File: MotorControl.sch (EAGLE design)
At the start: 47 parts, among them IC1 ESP32-WROOM-32E8M, IC2 TB6612FNG, U3 TP4056, U4 SPX3940AM3-L-3-3/TR, U5 INTERFACE-FT230XS-R(SSOP16)

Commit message: [fix] シルク作成
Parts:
- removed C17: 4.7uf, OPL_Capacitor:TANTALUM-SMD-4.7UF-16V(AVX-A)
- added C1: 100nf, OPL_Capacitor:CERAMIC-100NF-50V-10%-X7R(0805)
- C10: value 100nF/50V(10%) -> 4.7uf; device OPL_Capacitor:CERAMIC-100NF-50V-10%-X7R(0603) -> OPL_Capacitor:TANTALUM-SMD-4.7UF-16V(AVX-A)
- C2: value 100nf -> 10uf; device OPL_Capacitor:CERAMIC-100NF-50V-10%-X7R(0805) -> OPL_Capacitor:CERAMIC-10UF-25V-10%-X5R(1206)
- C3: value 10uf -> 22uF/16V(10%); device OPL_Capacitor:CERAMIC-10UF-25V-10%-X5R(1206) -> OPL_Capacitor:CERAMIC-22UF-16V-10%-X7R(1206)
- C4: value 22uF/16V(10%) -> 100nf; device OPL_Capacitor:CERAMIC-22UF-16V-10%-X7R(1206) -> OPL_Capacitor:CERAMIC-100NF-50V-10%-X7R(0805)
- C5: value 100nf -> 10nf; device OPL_Capacitor:CERAMIC-100NF-50V-10%-X7R(0805) -> OPL_Capacitor:CERAMIC-10NF-50V-5%-X7R(0805)
- C6: value 10nf -> 100nF/50V(10%); device OPL_Capacitor:CERAMIC-10NF-50V-5%-X7R(0805) -> OPL_Capacitor:CERAMIC-100NF-50V-10%-X7R(0603)
- renumbered BOOT_SW to BOOT-SW, D1 to BAT-RED, D2 to USB-TO-SERIAL-LED, D3 to PWR-LED, D4 to BAT-BLUE, E1 to FERRITE-BEAD, F1 to HUSE, IC1 to ESP32, IC2 to DRIVER-IC, MOTOR_PIN to MOTOR-PIN, POWER_SW to PWR-SW, R13 to R5, U3 to CHARGER-IC, U4 to LDO-IC, U5 to CNV-IC
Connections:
- net +3V3: now also C3.2, C6.2; no longer C4.2, C7.2
- net B+: now also C2.2; no longer C3.2
- net GND: now also C1.1, C10.-, C5.2, C6.1; no longer C10.1, C17.-, C5.1, C6.2
- net N$19: now also C10.+; no longer C17.+
- net N$29: now also C7.2; no longer C10.2
- net N$5: now also C4.2; no longer C5.2
- net VBUS: now also C5.1; no longer C6.1
- net VIN+: now also C1.2; no longer C2.2
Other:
- moved on the sheet: C2, C3, C4, C5, C6, C7

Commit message: [Fix] 20210920MT時点（４層）
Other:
- moved on the sheet: BAT-BLUE, BAT-RED, BOOT-SW, C1, C10, C11, C12, C13, C14, C15, C16, C2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

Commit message: [M] ２面に対応
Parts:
- removed R12, R9: 0.1R, OPL_Resistor:SMD-RES-0.1R-5%-1/8W(0805)
- added C17: 10UF 6.3V, OPL_Capacitor:CERAMIC-10UF-6.3V-20%-X5R(0603)
- added IC1: DW01A, DW01A:DW01A
- added Q1: FS8205A, FS8205A:FS8205A
- C13: value 10uf -> 100nf; device OPL_Capacitor:CERAMIC-10UF-25V-10%-X5R(0805) -> OPL_Capacitor:CERAMIC-100NF-50V-10%-X7R(0805)
- R5: value 0.1R -> 100R; device OPL_Resistor:SMD-RES-0.1R-5%-1/8W(0805) -> OPL_Resistor:SMD-RES-100R-5%-1/4W(1206)
- R8: value 0.1R -> 1K; device OPL_Resistor:SMD-RES-0.1R-5%-1/8W(0805) -> OPL_Resistor:SMD-RES-1K-5%-1/8W(0805)
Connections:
- removed net N$17: R8.2, R9.1
- removed net N$20: R12.2, R5.1
- new net B-: BAT.P$2, C13.2, IC1.GND, Q1.S1
- new net N$1: IC1.OC, Q1.G2
- new net N$10: IC1.OD, Q1.G1
- net B+: now also C17.1, R5.2; no longer C13.2
- net GND: now also C17.2, Q1.S2, R8.2; no longer BAT.P$2, C13.1
- net N$18: now also C13.1, IC1.VCC, R5.1; no longer R12.1, R9.2
- net N$19: now also IC1.CS; no longer C10.+, C16.2, CNV-IC.VCC, FERRITE-BEAD.1, R7.2
- net VIN+: now also C10.+, C16.2, CNV-IC.VCC, FERRITE-BEAD.1, R7.2; no longer R5.2
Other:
- moved on the sheet: BAT, BAT-BLUE, BAT-RED, C1, C13, CHARGER-IC, R2, R3, R5, R8, RPROG

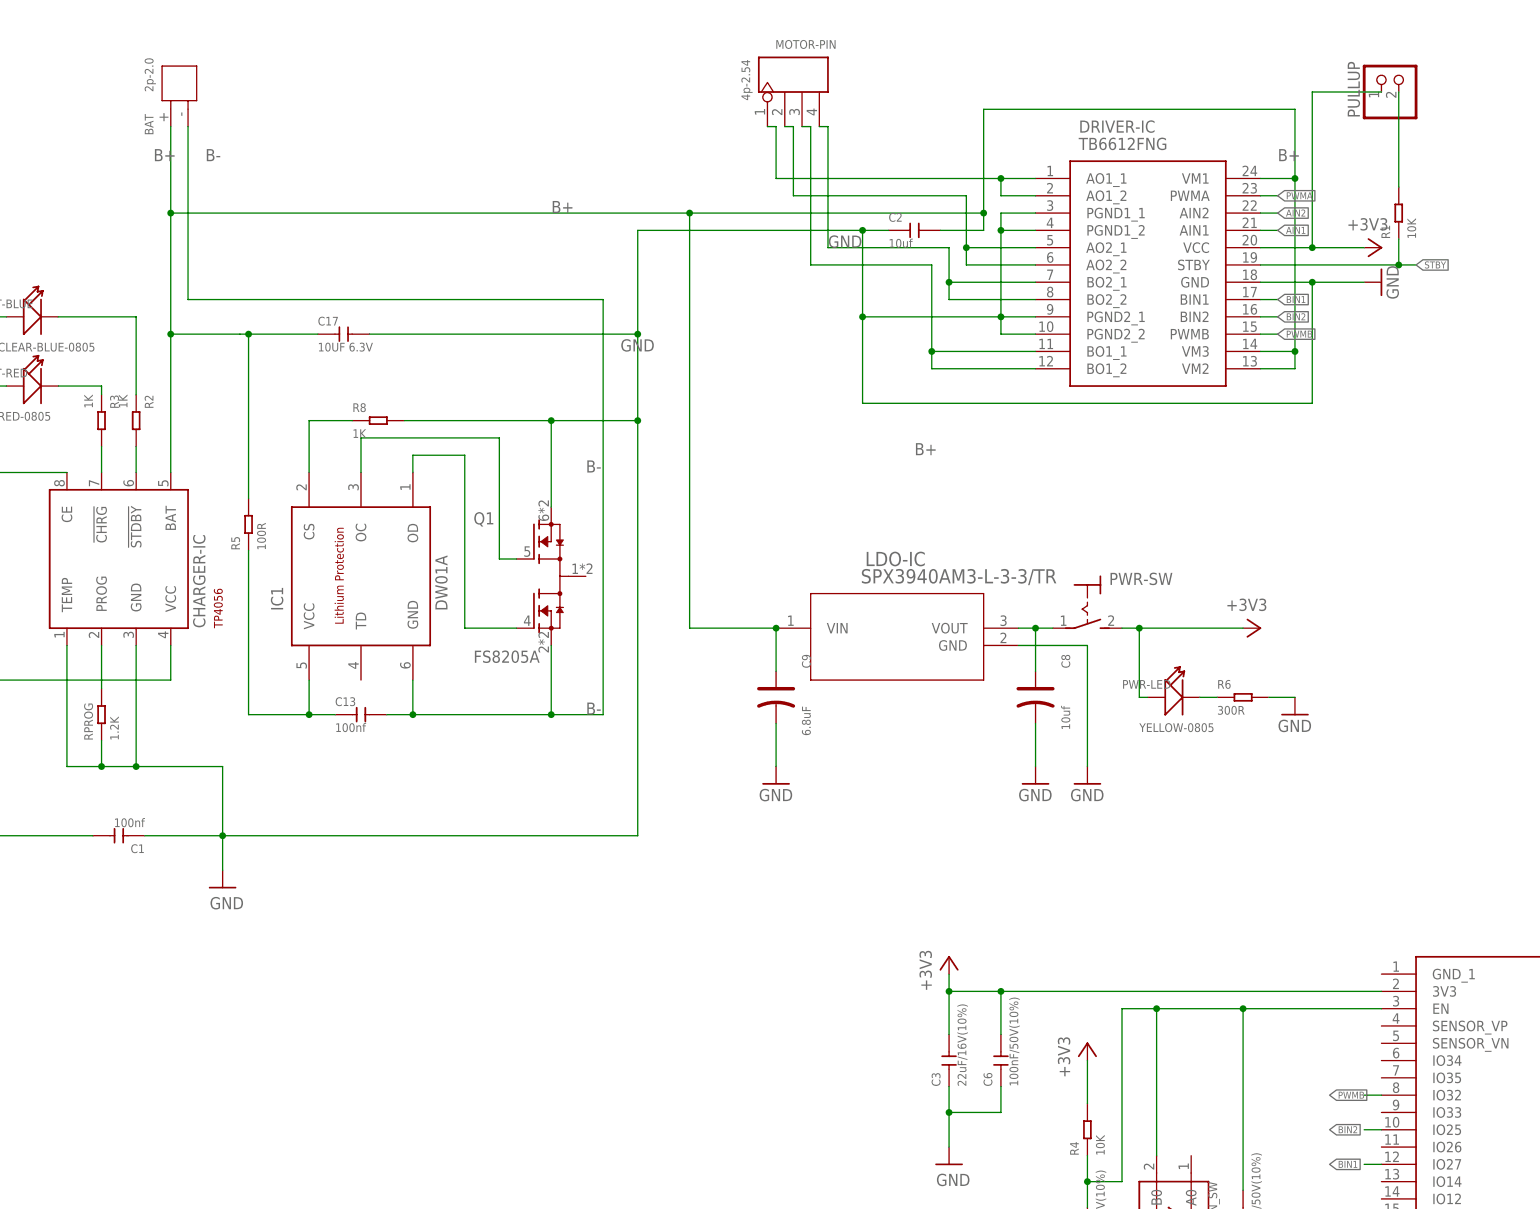
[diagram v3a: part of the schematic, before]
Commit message: [A] add output data
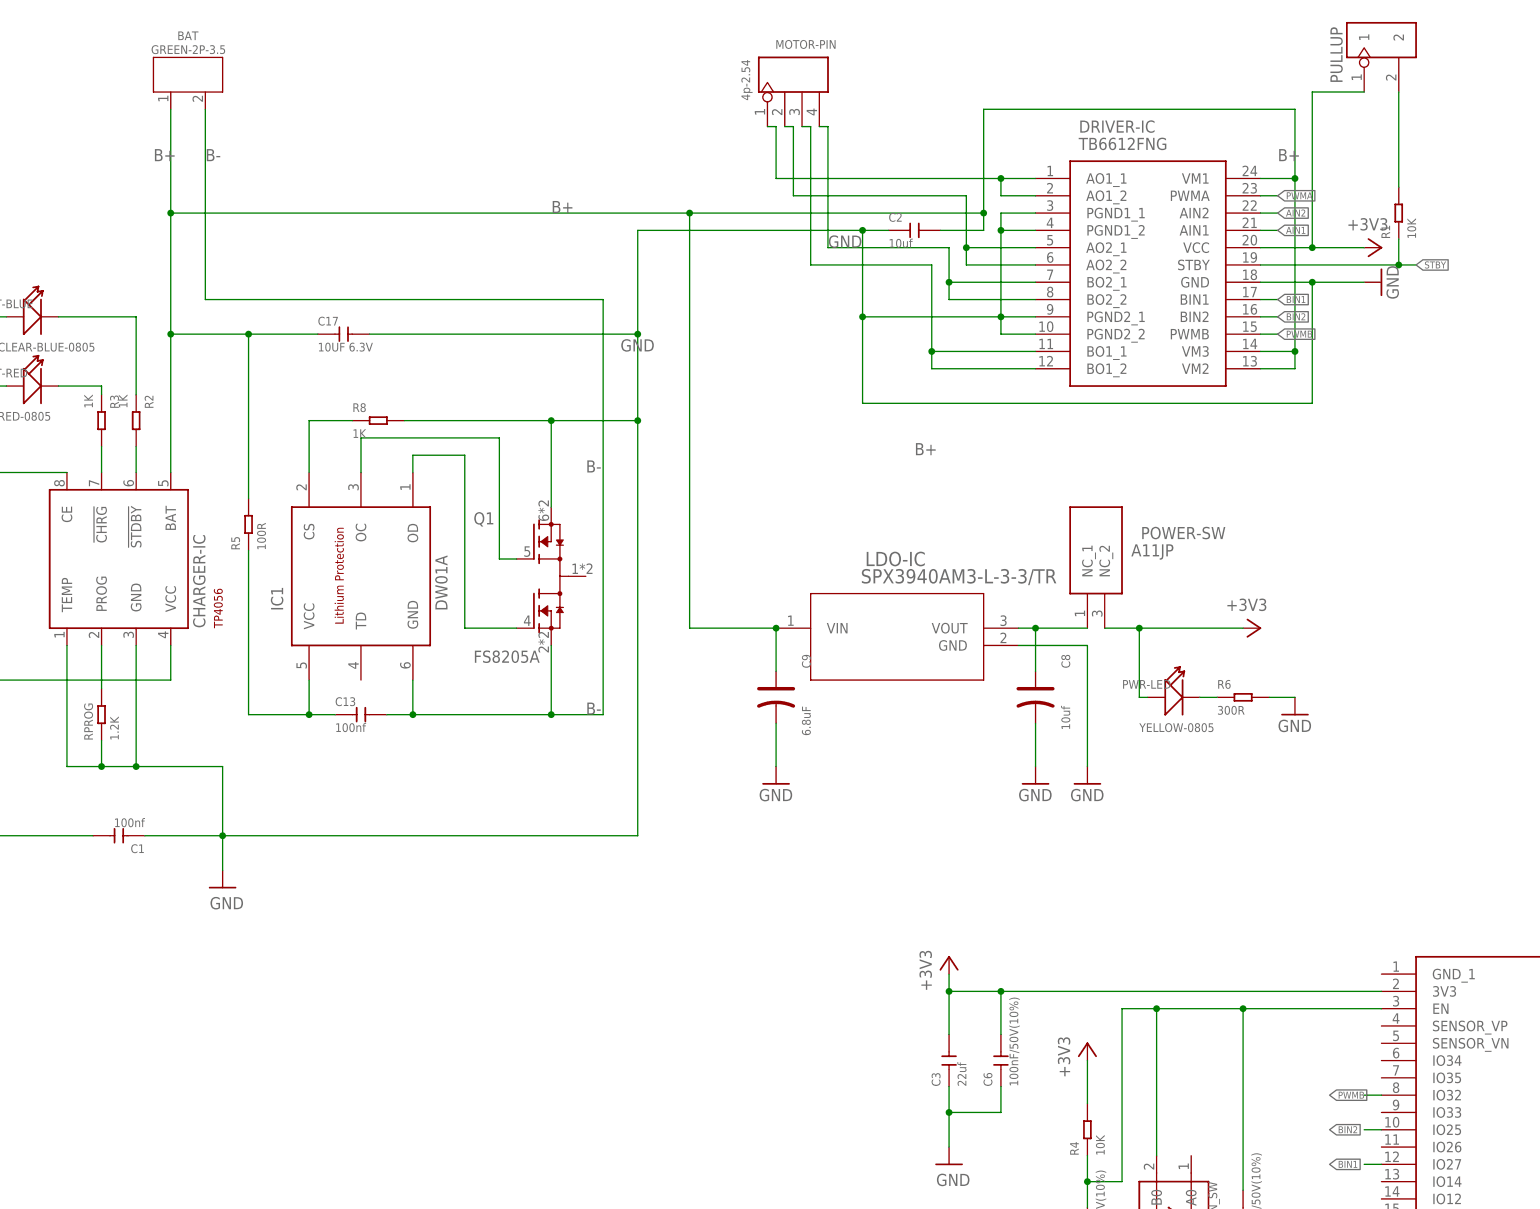
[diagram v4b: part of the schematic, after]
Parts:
- removed PWR-SW: (no value), switch:MS243
- added POWER-SW: A11JP, A11JP:A11JP
- BAT: value 2p-2.0 -> GREEN-2P-3.5; device OPL_Connector:DIP-JST-2P-2.0 -> OPL_Connector:SCREW-TERMINAL-GREEN(2P-3.5)
- C3: value 22uF/16V(10%) -> 22uf; device OPL_Capacitor:CERAMIC-22UF-16V-10%-X7R(1206) -> OPL_Capacitor:CERAMIC-22UF-6.3V-20%-X5R(0805)
- CHARGER-IC: MPN (none) -> TP4056
- HUSE: MPN (none) -> SMD0805R035SF
- PULLUP: device pinhead:PINHD-1X2 -> OPL_Connector:DIP-BLACK-JUMPER
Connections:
- net +3V3: now also POWER-SW.NC_2; no longer PWR-SW.S
- net B+: now also BAT.1; no longer BAT.P$1
- net B-: now also BAT.2; no longer BAT.P$2
- net POWER_SW: now also POWER-SW.NC_1; no longer PWR-SW.P
